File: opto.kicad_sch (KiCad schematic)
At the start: 18 parts, among them J5 UART_Device, U1 SN74LVC1G17DBVR, U10 TLP2361(TPL,E(T, U5 SN74LVC1G17DBVR, U8 SN74LVC1G17DBVR, U9 TLP2361(TPL,E(T

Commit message: Rework the opto circuit with smaller caps to reduce clutter.
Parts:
- C1, C2, C20, C21, C22: symbol Device:C -> Device:C_Small
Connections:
- net at U10.3: now also R23.1
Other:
- moved on the sheet: C1, C2, C20, C21, C22, R11, R23, U1, U5, U8

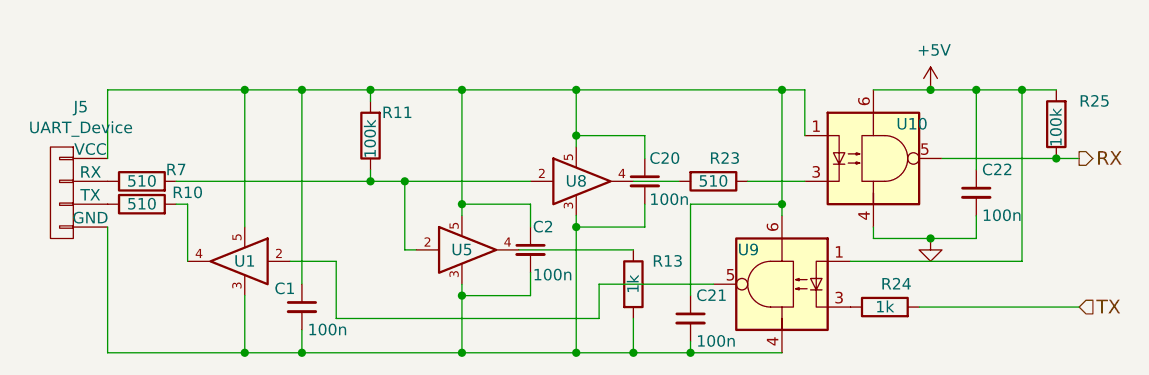
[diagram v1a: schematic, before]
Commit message: Use standard format for resistor values
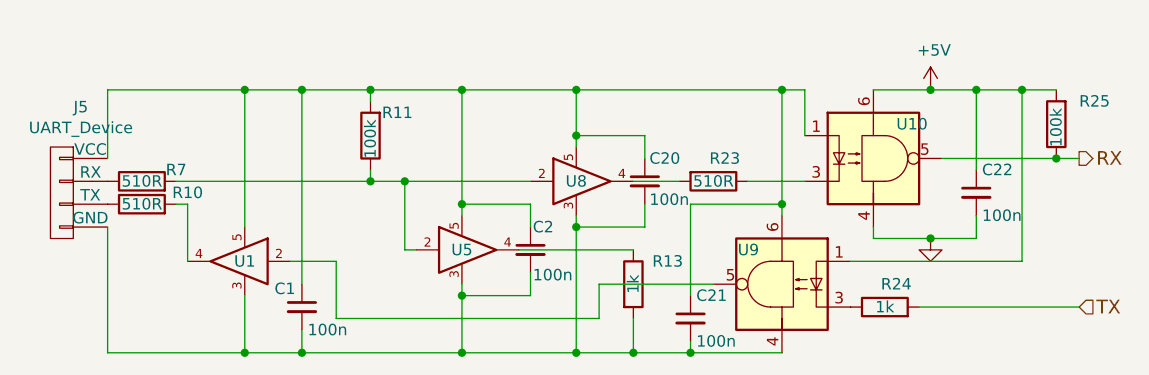
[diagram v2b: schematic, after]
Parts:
- R10, R23, R7: value 510 -> 510R
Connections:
- net at U10.3: now also R23.1
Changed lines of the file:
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@@
 			)
 		)
-		(property "Value" "510"
+		(property "Value" "510R"
 			(at 101.6 45.72 90)
 			(effects
@@
 			)
 		)
-		(property "Value" "510"
+		(property "Value" "510R"
 			(at 165.1 43.18 90)
 			(effects
@@
 			)
 		)
-		(property "Value" "510"
+		(property "Value" "510R"
 			(at 101.6 43.18 90)
 			(effects

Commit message: Added version numbers to make variants easier to make
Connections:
- net at U10.3: now also R23.1
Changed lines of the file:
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@@
 	(generator_version "8.0")
 	(paper "A4")
+	(title_block
+		(date "19-Dec-2024")
+		(rev "3.0a")
+	)
 	(junction
 		(at 113.03 33.02)

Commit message: Updating U9/U10 opto symbols pulled symbol into .kicad_sch file
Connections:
- net at U10.3: now also R23.1
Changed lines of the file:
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@@
 	)
 	(symbol
+		(lib_name "tlp2361_1")
 		(lib_id "pypilot_components:tlp2361")
 		(at 172.72 54.61 0)

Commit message: Move hidden pin 1 to align to grid (removes ERC warning)
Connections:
- net at U10.3: now also R23.1

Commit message: eeschema wants this cached copy of the tlp2361 gone
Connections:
- net at U10.3: now also R23.1
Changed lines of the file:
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@@
 	)
 	(symbol
-		(lib_name "tlp2361_1")
+		(lib_name "pypilot_components:tlp2361")
 		(lib_id "pypilot_components:tlp2361")
 		(at 172.72 54.61 0)

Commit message: Change TO-252 footprint to use less solder paste
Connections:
- net at U10.3: now also R23.1
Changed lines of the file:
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@@
 	)
 	(symbol
-		(lib_name "pypilot_components:tlp2361")
 		(lib_id "pypilot_components:tlp2361")
 		(at 172.72 54.61 0)

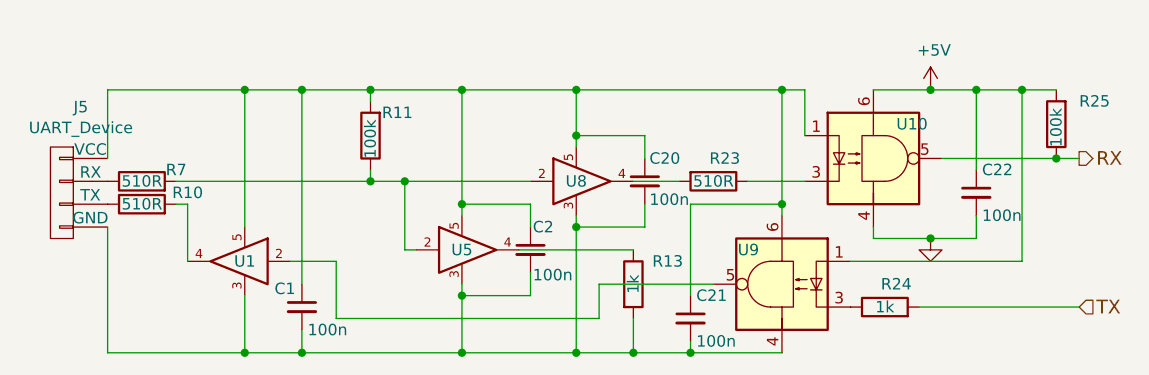
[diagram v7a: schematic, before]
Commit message: Fixed almost all ERC errors and warnings (now 0 errors, 3 warnings)
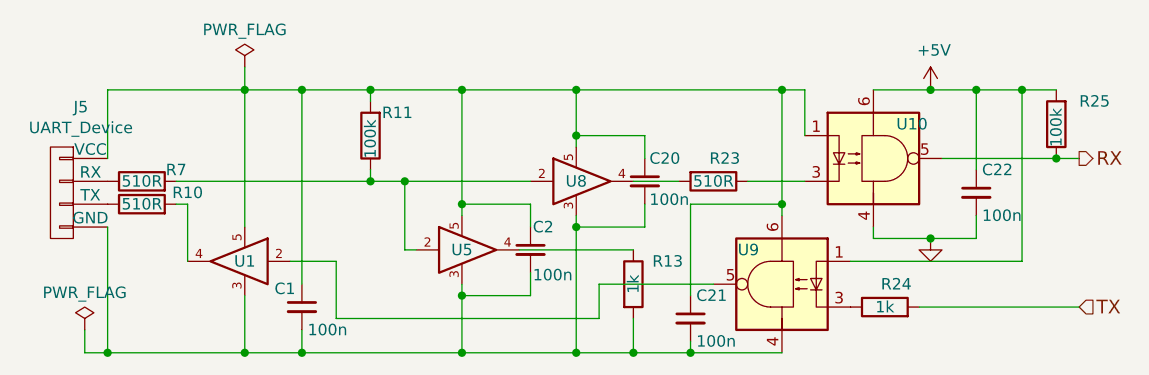
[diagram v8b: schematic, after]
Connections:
- net at U10.3: now also R23.1
